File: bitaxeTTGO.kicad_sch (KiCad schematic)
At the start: 8 parts, among them J1 Conn_01x01, J2 Conn_01x01

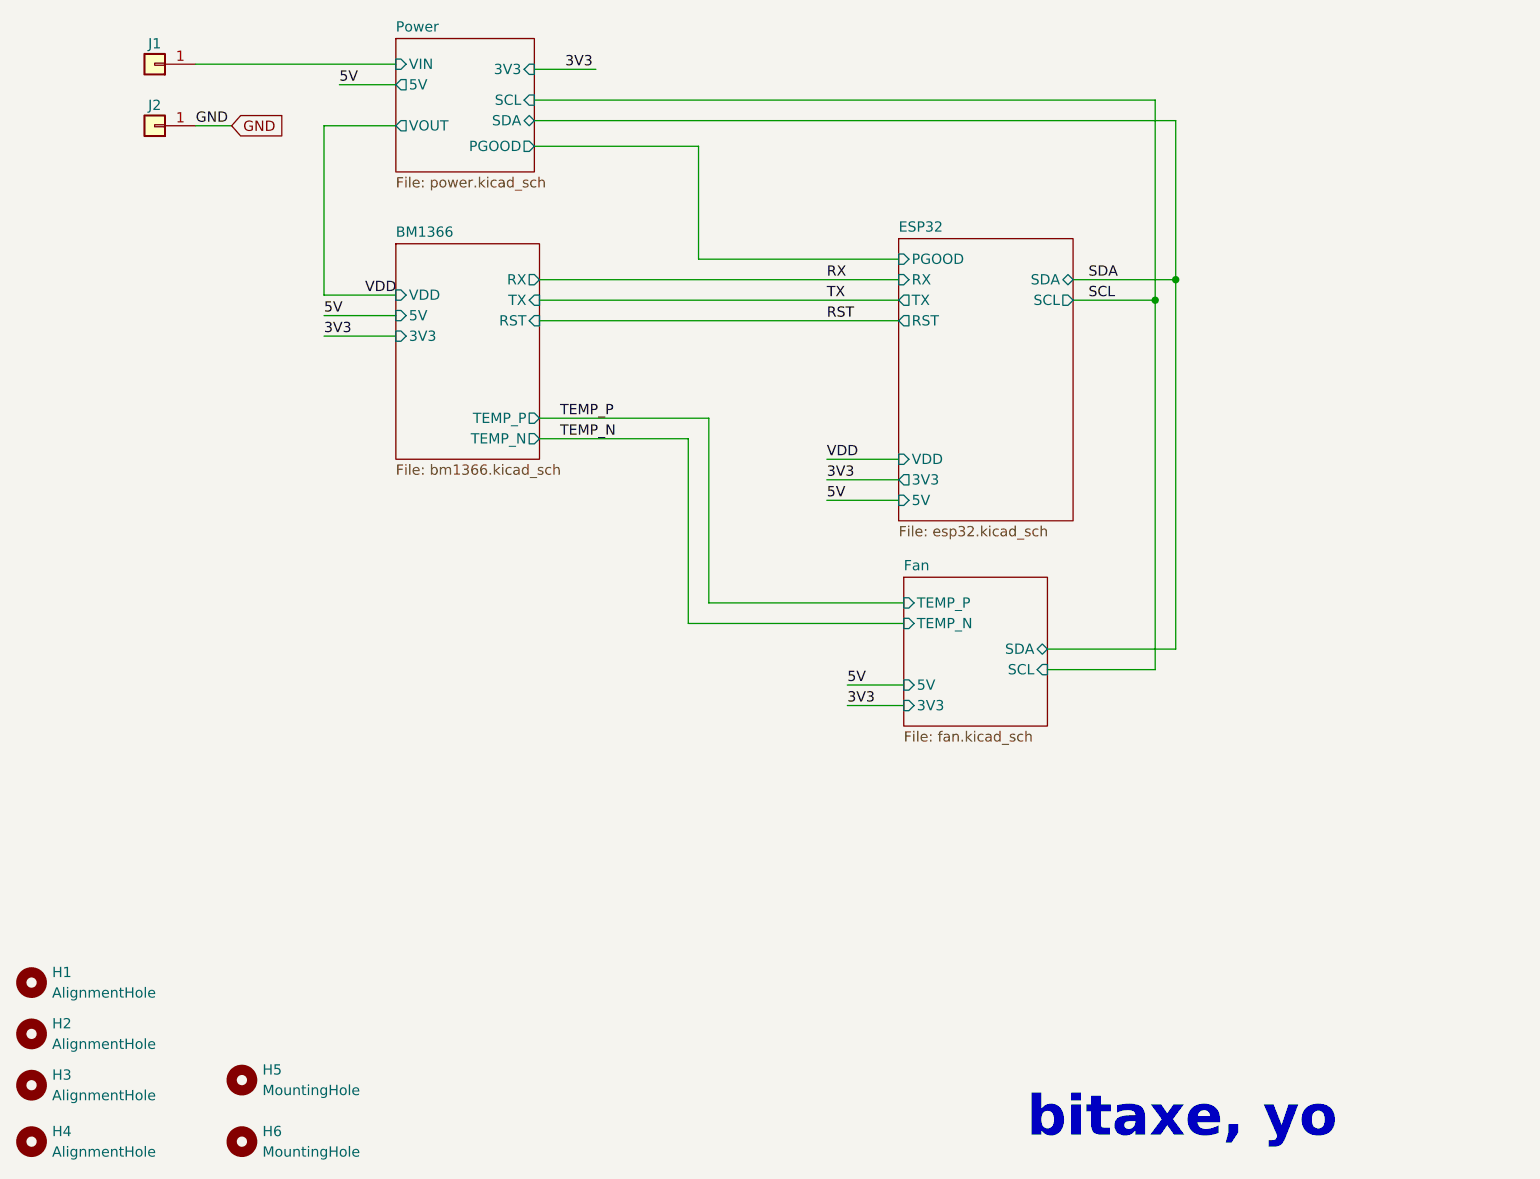
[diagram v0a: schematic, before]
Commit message: added T-Display-S3 and barrel connector
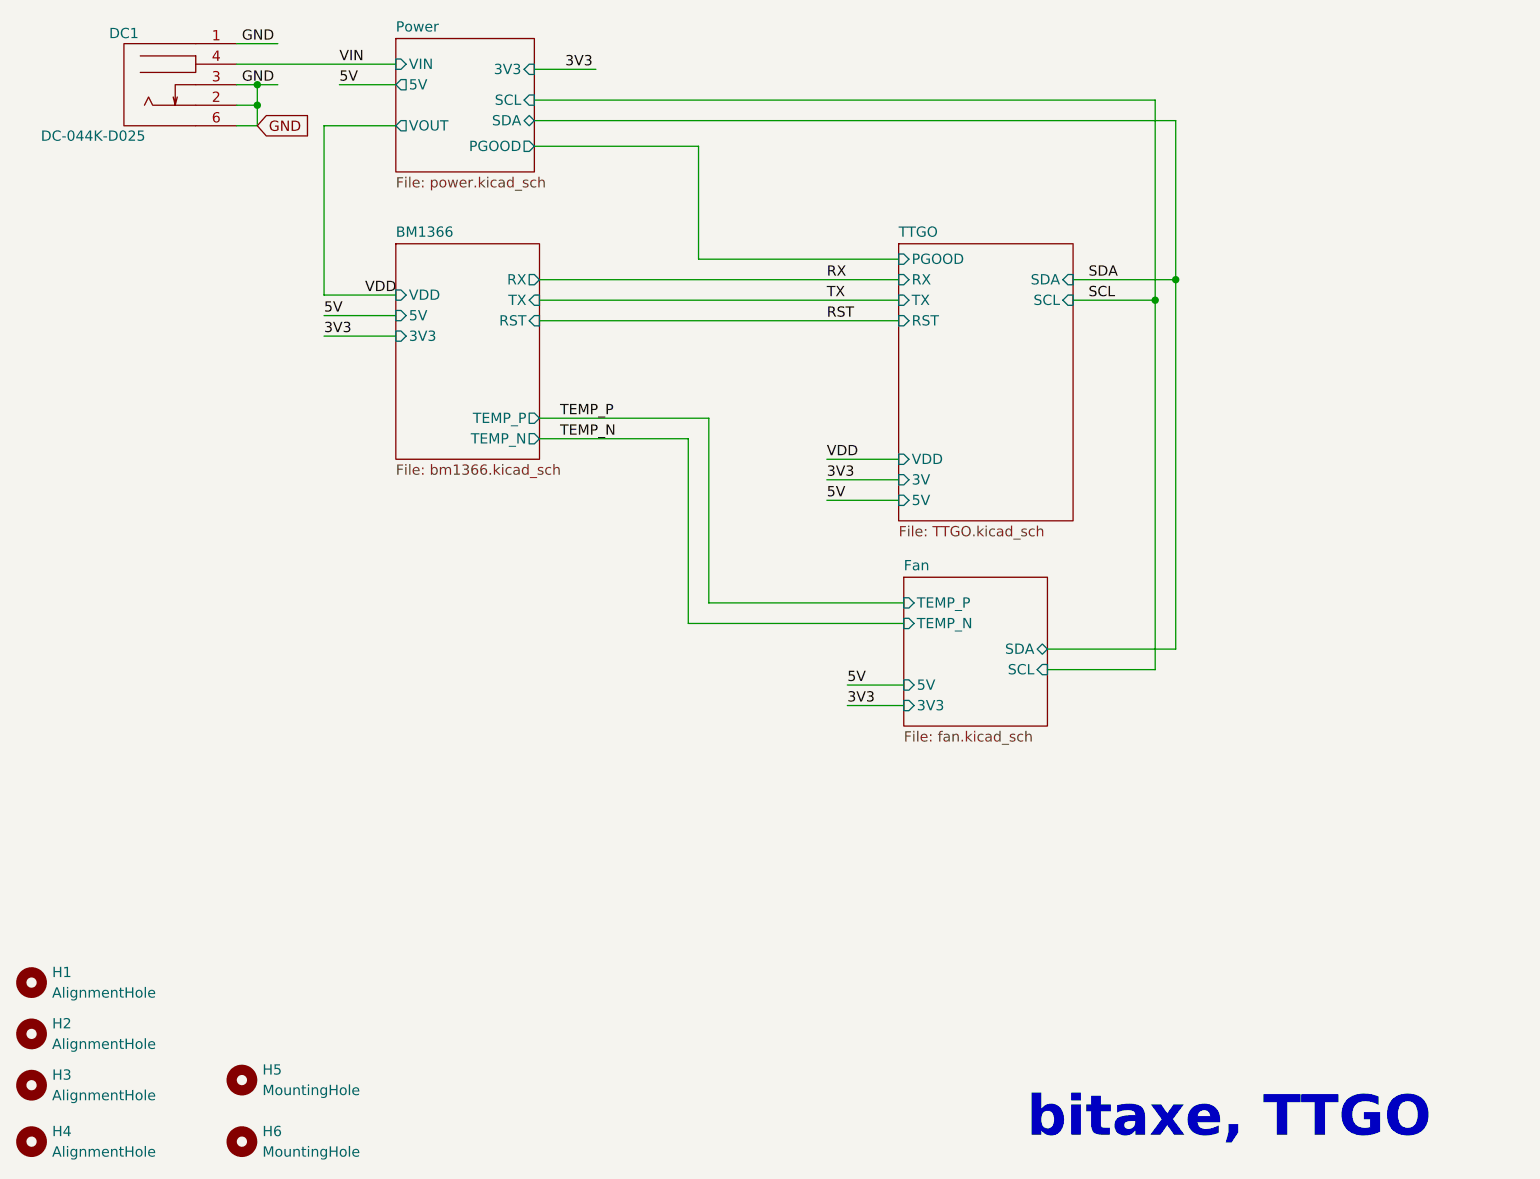
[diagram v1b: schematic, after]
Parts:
- removed J1, J2: Conn_01x01, TPS40305_supply:63862-1, symbol Connector_Generic:Conn_01x01
- added DC1: DC-044K-D025, lcsc:DC-IN-TH_DC-044K-D025, symbol lcsc:DC-044K-D025
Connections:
- net GND: now also DC1.1, DC1.2, DC1.3, DC1.6
- new net VIN: DC1.4
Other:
- removed sheet ESP32
- added sheet TTGO (TTGO.kicad_sch)
- note added: "bitaxe, TTGO"
- note removed: "bitaxe, yo"
- title: le bitaxeUltra -> le bitaxeTTGO
